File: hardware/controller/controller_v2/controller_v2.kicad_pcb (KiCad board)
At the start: 2 copper layers, 48.5 x 38.5 mm, 22 parts, among them J1 USB_C_Receptacle_USB2.0_16P, J2 Conn_01x04_Socket, SW1 SW_Push, SW2 SW_Push, U1 ESP32-C3-MINI-1-N4, U2 74AHCT1G125, U4 AMS1117-3.3

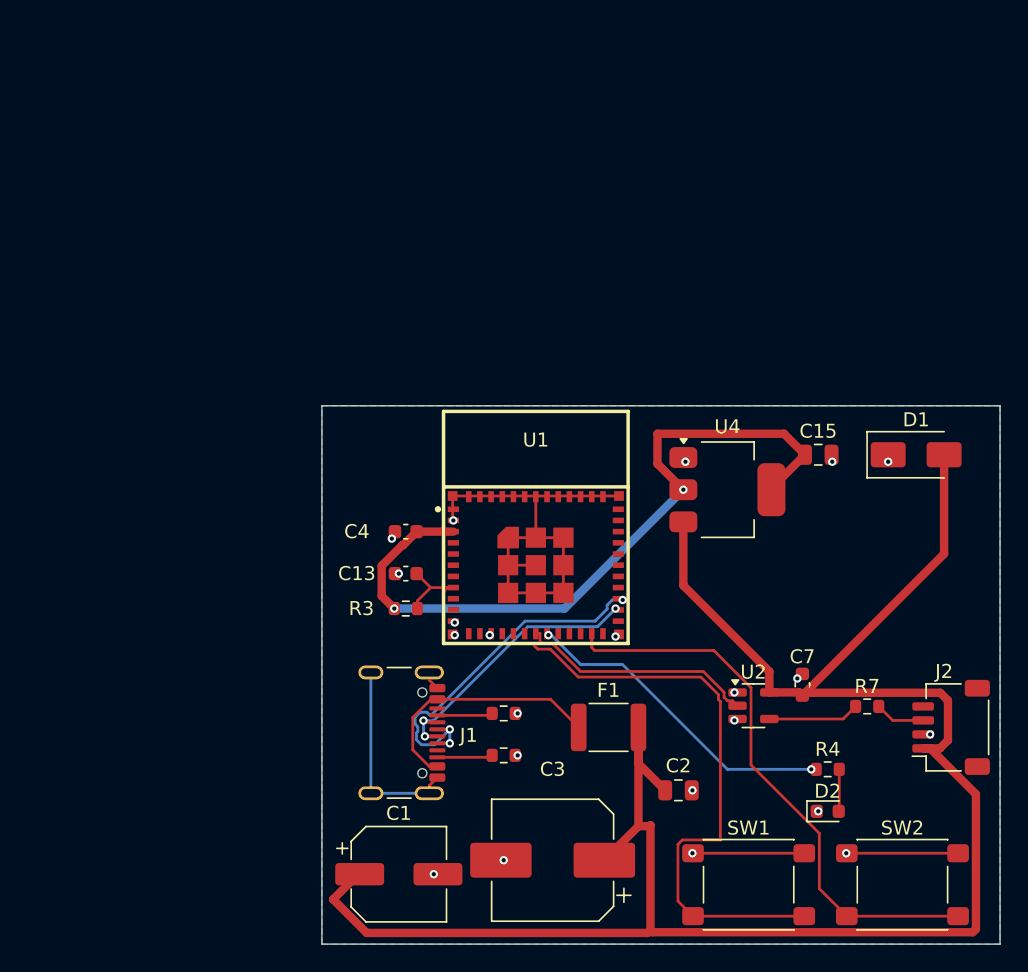
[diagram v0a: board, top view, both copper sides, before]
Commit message: Hardware: finalize controller v2 + add octave-flex design
Controller v2 (ready for JLCPCB assembly):
- DRC clean, all clearance/footprint issues resolved
- U3 (TS3USB221A QFN-10) fine-pitch handling: local clearance override + solder_mask_margin=0 on all pads
- J4 PJ-320A footprint update + mechanical pad fix (1.2mm -> 1.6mm)
- C14 removed (redundant with C3 470uF bulk near J2)
- BOM verified with LCSC part numbers, all 26 SMT parts vetted for JLC matching
- Gerbers + production files exported via Fabrication Toolkit

New octave-flex design (replaces 5x rigid octave-module):
- Single 829.35 x 10.69 mm flex PCB, 60 LEDs at 13.75mm uniform spacing
- WS2812B 5050 footprint, J1 (JST SH 4P) connector at left edge
- GND zone (hatched, 45-degree, 0.5/0.5mm) on B.Cu - flex-compatible
- FR-4 stiffener spec under J1 for PCBWay
- 60 LED + 60 cap + 1 connector hand-solderable

BOM.csv updates:
- C3 promoted to 470uF aluminum bulk (was 0.1uF spare)
- C7 added as spare 5V decoupling
- Octave entries replaced: D1-D60 + C1-C60 + J1 single flex board
- Cabling: 5 cables -> 1 cable (single strip vs 5 boards)

Co-Authored-By: Claude Opus 4.7 <noreply@anthropic.com>
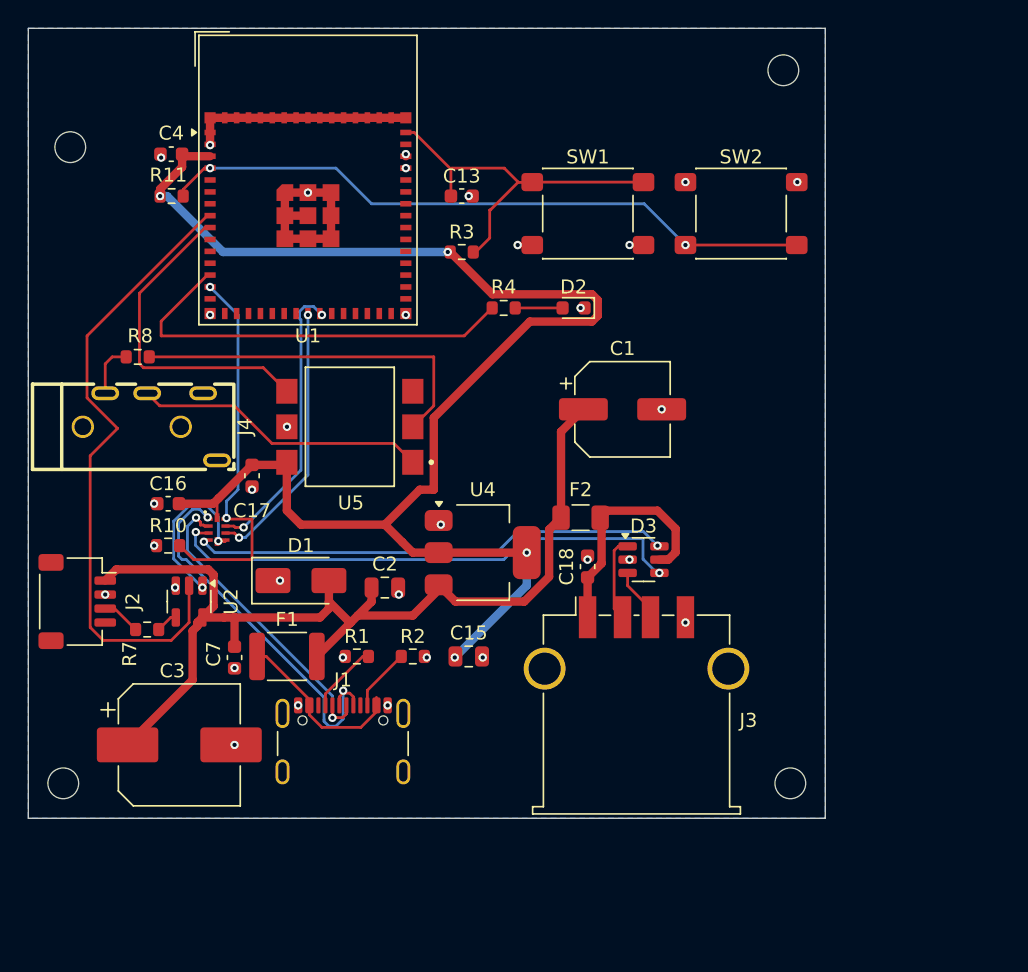
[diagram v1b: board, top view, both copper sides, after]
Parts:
- added C16: 0.1uF, Capacitor_SMD:C_0603_1608Metric, F.Cu at (110.0, 89.0)
- added C17: 0.1uF, Capacitor_SMD:C_0603_1608Metric, F.Cu at (116.0, 87.0)
- added C18: 0.1uF, Capacitor_SMD:C_0603_1608Metric, F.Cu at (140.0, 93.5)
- added D3: USBLC6-2SC6, Package_TO_SOT_SMD:SOT-23-6, F.Cu at (144.0, 93.0)
- added F2: 500mA, Fuse:Fuse_1206_3216Metric, F.Cu at (139.5, 90.0)
- added J3: USB_A, Connector_USB:USB_A_TE_292303-7_Horizontal, F.Cu at (143.5, 103.5)
- added J4: PJ-320A, easyeda2kicad:AUDIO-TH_XKB_PJ-320A, F.Cu at (109.5, 83.5)
- added R10: 10k, Resistor_SMD:R_0603_1608Metric, F.Cu at (110.0, 92.0)
- added R11: 10k, Resistor_SMD:R_0603_1608Metric, F.Cu at (110.2, 67.0)
- added R8: 220, Resistor_SMD:R_0603_1608Metric, F.Cu at (107.8, 78.5)
- added REF**: MountingHole_2.2mm_M2, MountingHole:MountingHole_2.2mm_M2, F.Cu at (103.0, 63.5)
- added REF**: MountingHole_2.2mm_M2, MountingHole:MountingHole_2.2mm_M2, F.Cu at (154.0, 58.0)
- added REF**: MountingHole_2.2mm_M2, MountingHole:MountingHole_2.2mm_M2, F.Cu at (154.5, 109.0)
- added REF**: MountingHole_2.2mm_M2, MountingHole:MountingHole_2.2mm_M2, F.Cu at (102.5, 109.0)
- added U3: TS3USB221A, TS3USB221A:QFN-10-RSE, F.Cu at (113.5, 90.8)
- added U5: H11L1, H11L1SM:IC_H11L1SM, F.Cu at (123.0, 83.5)
- U1: value ESP32-C3-MINI-1-N4 -> ESP32-S3-MINI-1; footprint ESP32-C3-MINI-1:WIFIM-SMD_ESP32-C3-MINI-1 -> RF_Module:ESP32-S2-MINI-1
- moved J2 63.1 mm to (103.5, 96.0), turned to -90 degrees
- moved R7 51.8 mm to (108.5, 98.0), turned to 180 degrees
- moved SW2 49.4 mm to (151.0, 68.2)
- moved SW1 49.4 mm to (140.0, 68.2)
- moved D1 44.9 mm to (119.5, 94.5)
- moved U2 41.0 mm to (111.5, 96.0), turned to -90 degrees
- moved C7 40.7 mm to (114.8, 100.0), turned to -90 degrees
- moved D2 40.3 mm to (139.0, 75.0), turned to 180 degrees
- moved R4 40.3 mm to (134.0, 75.0)
- moved C1 36.9 mm to (142.5, 82.2)
- moved U1 32.0 mm to (120.0, 65.8)
- moved C4 31.8 mm to (110.2, 64.0)
- moved C15 28.9 mm to (131.5, 99.9)
- moved C3 27.9 mm to (110.8, 106.2), turned to 0 degrees
- moved C13 27.3 mm to (131.0, 67.0), turned to 0 degrees
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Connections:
- C13 pad 1: Net-(U1-EN) -> /EN
- J1 pad A6: /D_P -> /USBC_DP
- J1 pad A7: /D_N -> /USBC_DM
- J1 pad B6: /D_P -> /USBC_DP
- J1 pad B7: /D_N -> /USBC_DM
- R3 pad 1: Net-(U1-EN) -> +3.3V
- R3 pad 2: +3.3V -> /EN
- R4 pad 1: Net-(U1-IO5) -> /STATUS
- SW1 pad 1: GND -> /EN
- SW1 pad 2: Net-(U1-EN) -> GND
- SW2 pad 2: Net-(U1-IO9) -> /BOOT
- U1 pad 11: GND -> unconnected-(U1-IO7-Pad11)
- U1 pad 13: unconnected-(U1-IO1-Pad13) -> /STATUS
- U1 pad 14: GND -> /USB_SEL
- U1 pad 18: /LED_DATA_3V3 -> unconnected-(U1-IO14-Pad18)
- U1 pad 19: Net-(U1-IO5) -> unconnected-(U1-IO15-Pad19)
- U1 pad 23: Net-(U1-IO9) -> /USB_DM
- U1 pad 24: unconnected-(U1-NC-Pad24) -> /USB_DP
- U1 pad 26: /D_N -> unconnected-(U1-IO26-Pad26)
- U1 pad 27: /D_P -> unconnected-(U1-IO47-Pad27)
- U1 pad 36: GND -> unconnected-(U1-IO40-Pad36)
- U1 pad 37: GND -> unconnected-(U1-IO41-Pad37)
- U1 pad 38: GND -> unconnected-(U1-IO42-Pad38)
- U1 pad 39: GND -> unconnected-(U1-TXD0-Pad39)
- U1 pad 4: unconnected-(U1-NC-Pad4) -> /BOOT
- U1 pad 40: GND -> unconnected-(U1-RXD0-Pad40)
- U1 pad 41: GND -> unconnected-(U1-IO45-Pad41)
- U1 pad 44: GND -> unconnected-(U1-IO46-Pad44)
- U1 pad 45: GND -> /EN
- U1 pad 8: Net-(U1-EN) -> /LED_DATA_3V3
- U1 pad 9: unconnected-(U1-NC-Pad9) -> /MIDI_RX
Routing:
- net +5V: track 143.0 -> 74.1 mm
- net Net-(U1-EN): track 57.9 -> 0.00 mm
- net +3.3V: track 53.2 -> 107.6 mm, vias 2 -> 4
- net /BOOT: track 0.00 -> 47.3 mm, vias 0 -> 2
- net Net-(U1-IO9): track 40.7 -> 0.00 mm
- net /USBA_DP: track 0.00 -> 38.0 mm, vias 0 -> 2
- net /USBA_DM: track 0.00 -> 34.4 mm, vias 0 -> 2
- net /STATUS: track 0.00 -> 30.4 mm
- net /LED_DATA_3V3: track 17.2 -> 45.5 mm
- net /USB_SEL: track 0.00 -> 28.2 mm, vias 0 -> 2
- net /USBC_DP: track 0.00 -> 27.9 mm, vias 0 -> 2
- net /EN: track 0.00 -> 26.9 mm
- net /D_P: track 26.5 -> 0.00 mm, vias 3 -> 0
- net Net-(R8-Pad2): track 0.00 -> 26.0 mm
- net /USBC_DM: track 0.00 -> 23.5 mm, vias 0 -> 2
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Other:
- board size 48.5 x 38.5 mm -> 57 x 56.5 mm

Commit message: Octave-module flex PCB ready for fab; checkpoint full repo
hardware/octave-module: uniform 13.708 mm LED pitch (caps aligned), solder lap-seam (J2 output / J3 input pads), J2 plated 0.8 mm solder-access holes, full routing + GND pour, J1 placement; seam-lap footprint library; spacing/seam design docs; regenerated BOM + production files (J1 DNP, caps C14663, LEDs C2761795).
Also includes controller_v2, mobile app, backend, and project-doc updates.

Co-Authored-By: Claude Opus 4.8 <noreply@anthropic.com>
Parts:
- added R12: 1k, Resistor_SMD:R_0603_1608Metric, F.Cu at (133.3, 84.5)
- J3: footprint Connector_USB:USB_A_TE_292303-7_Horizontal -> easyeda2kicad:USB-A-TH__USB-AF-90
- SW1, SW2: footprint Button_Switch_SMD:SW_SPST_PTS645Sx43SMTR92 -> easyeda2kicad:SW-SMD_4P-L5.1-W5.1-P3.70-LS6.5-TL_H1.5
- moved J3 3.90 mm to (142.8, 99.7)
- moved SW1 1.56 mm to (141.1, 67.1)
- moved SW2 1.20 mm to (150.6, 67.1)
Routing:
- net /MIDI_RX: track 23.4 -> 49.0 mm, vias 0 -> 2
- net Net-(R8-Pad2): track 26.0 -> 30.2 mm
- net +3.3V: track 107.6 -> 111.8 mm
- net Net-(D3-VBUS): track 16.8 -> 18.3 mm
- net Net-(J3-D-): track 6.11 -> 7.56 mm
- net /BOOT: track 47.3 -> 46.0 mm
- net Net-(J3-D+): track 3.85 -> 4.75 mm
- net GND: track 49.2 -> 49.1 mm, vias 35 -> 34
